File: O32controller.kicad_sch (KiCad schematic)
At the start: 25 parts, among them J1 Conn_01x08_MountingPin, J2 BATT+, J3 BATT-, J7 BATT+, J8 BATT-, U1 AS5047D, U2 STSPIN32F0A

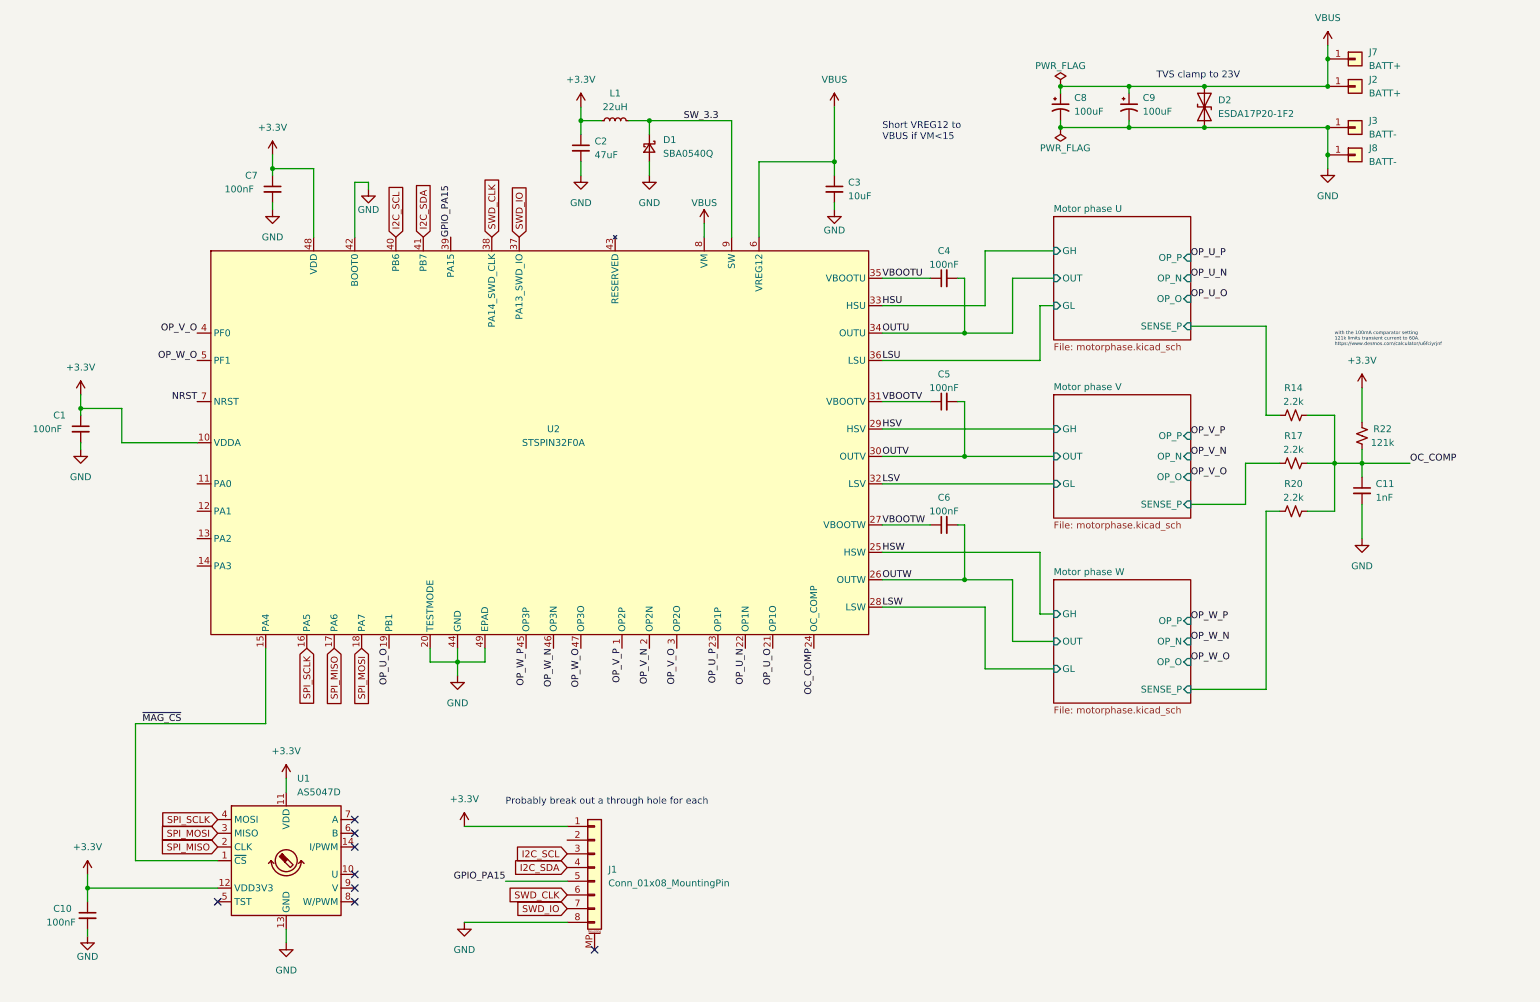
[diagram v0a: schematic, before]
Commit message: assigned gpio and adcs
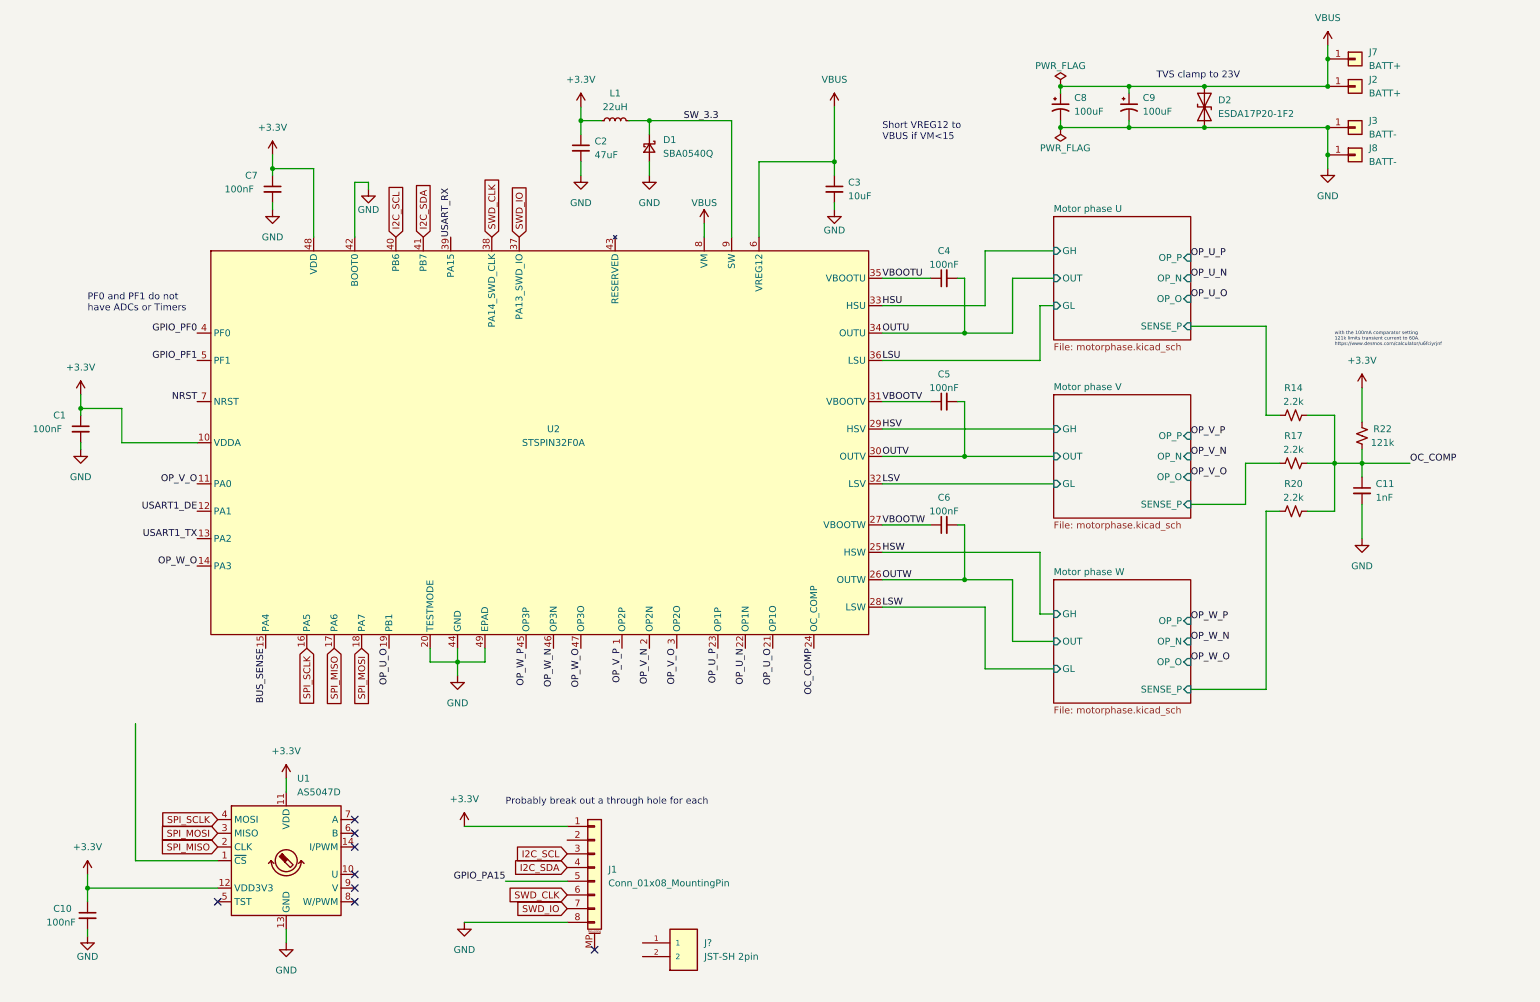
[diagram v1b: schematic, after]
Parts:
- added J?: JST-SH 2pin, SM02B-SRSS-TB(LF)(SN), symbol O32controller:SM02B-SRSS-TB(LF)(SN)
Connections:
- net GPIO_PA15: no longer U2.39 (PA15)
- net OP_V_O: now also U2.11 (PA0); no longer U2.4 (PF0)
- net OP_W_O: now also U2.14 (PA3); no longer U2.5 (PF1)
- net USART1_DE: now reaches U2.12 (PA1)
- net USART1_TX: now reaches U2.13 (PA2)
- net ~{MAG_CS}: no longer names the net of U1.1 (~{CS})
- net ~{MAG_CS}: no longer U2.15 (PA4)
- new net BUS_SENSE: U2.15 (PA4)
- new net GPIO_PF0: U2.4 (PF0)
- new net GPIO_PF1: U2.5 (PF1)
- new net USART_RX: U2.39 (PA15)
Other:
- note added: "PF0 and PF1 do not have ADCs or Timers"
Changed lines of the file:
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@@
-    (stroke (width 0) (type default) (color 0 0 0 0))
-  )
-  (wire (pts (xy 58.42 146.05) (xy 58.42 132.08))
     (stroke (width 0) (type default) (color 0 0 0 0))
   )
@@
     (stroke (width 0) (type default) (color 0 0 0 0))
   )
-  (wire (pts (xy 34.29 146.05) (xy 58.42 146.05))
-    (stroke (width 0) (type default) (color 0 0 0 0))
-  )
   (wire (pts (xy 204.47 130.81) (xy 196.85 130.81))
     (stroke (width 0) (type default) (color 0 0 0 0))
@@
   (wire (pts (xy 172.72 91.44) (xy 204.47 91.44))
     (stroke (width 0) (type default) (color 0 0 0 0))
+  )
+  (text "PF0 and PF1 do not \nhave ADCs or Timers\n" (at 25.4 69.85 0)
+    (effects (font (size 1.27 1.27)) (justify left bottom))
   )
   (text "Short VREG12 to \nVBUS if VM<15" (at 172.72 38.1 0)
@@
     (effects (font (size 1.27 1.27)) (justify right bottom))
   )
-  (label "OP_W_O" (at 45.72 78.74 180)
-    (effects (font (size 1.27 1.27)) (justify right bottom))
-  )
   (label "OP_V_N" (at 229.87 96.52 0)
     (effects (font (size 1.27 1.27)) (justify left bottom))
@@
     (effects (font (size 1.27 1.27)) (justify left bottom))
   )
-  (label "GPIO_PA15" (at 92.71 55.88 90)
-    (effects (font (size 1.27 1.27)) (justify left bottom))
-  )
   (label "OC_COMP" (at 160.02 132.08 270)
     (effects (font (size 1.27 1.27)) (justify right bottom))
@@
     (effects (font (size 1.27 1.27)) (justify left bottom))
   )
+  (label "GPIO_PF1" (at 45.72 78.74 180)
+    (effects (font (size 1.27 1.27)) (justify right bottom))
+  )
+  (label "USART1_DE" (at 45.72 106.68 180)
+    (effects (font (size 1.27 1.27)) (justify right bottom))
+  )
   (label "VBOOTW" (at 172.72 109.22 0)
     (effects (font (size 1.27 1.27)) (justify left bottom))
   )
+  (label "BUS_SENSE" (at 58.42 132.08 270)
+    (effects (font (size 1.27 1.27)) (justify right bottom))
+  )
   (label "NRST" (at 45.72 86.36 180)
     (effects (font (size 1.27 1.27)) (justify right bottom))
   )
+  (label "GPIO_PF0" (at 45.72 73.66 180)
+    (effects (font (size 1.27 1.27)) (justify right bottom))
+  )
   (label "LSU" (at 172.72 78.74 0)
     (effects (font (size 1.27 1.27)) (justify left bottom))
@@
     (effects (font (size 1.27 1.27)) (justify left bottom))
   )
-  (label "~{MAG_CS}" (at 35.56 146.05 0)
-    (effects (font (size 1.27 1.27)) (justify left bottom))
-  )
   (label "HSU" (at 172.72 68.58 0)
     (effects (font (size 1.27 1.27)) (justify left bottom))
   )
+  (label "USART_RX" (at 92.71 55.88 90)
+    (effects (font (size 1.27 1.27)) (justify left bottom))
+  )
   (label "OP_U_O" (at 152.4 132.08 270)
     (effects (font (size 1.27 1.27)) (justify right bottom))
@@
     (effects (font (size 1.27 1.27)) (justify left bottom))
   )
+  (label "OP_W_O" (at 45.72 116.84 180)
+    (effects (font (size 1.27 1.27)) (justify right bottom))
+  )
   (label "VBOOTV" (at 172.72 86.36 0)
     (effects (font (size 1.27 1.27)) (justify left bottom))
@@
     (effects (font (size 1.27 1.27)) (justify left bottom))
   )
-  (label "OP_V_O" (at 45.72 73.66 180)
+  (label "OP_V_O" (at 45.72 101.6 180)
     (effects (font (size 1.27 1.27)) (justify right bottom))
   )
@@
   (label "OUTW" (at 172.72 119.38 0)
     (effects (font (size 1.27 1.27)) (justify left bottom))
+  )
+  (label "USART1_TX" (at 45.72 111.76 180)
+    (effects (font (size 1.27 1.27)) (justify right bottom))
   )
   (global_label "SWD_IO" (shape input) (at 114.3 180.34 180) (fields_autoplaced)
@@
     (pin "MP")
   )
+  (symbol (lib_id "O32controller:SM02B-SRSS-TB(LF)(SN)") (at 128.27 191.77 0) (unit 1)
+    (in_bom yes) (on_board yes) (fields_autoplaced)
+    (property "Reference" "J?" (id 0) (at 139.7 186.6899 0)
+      (effects (font (size 1.27 1.27)) (justify left))
+    )
+    (property "Value" "JST-SH 2pin" (id 1) (at 139.7 189.2299 0)
+      (effects (font (size 1.27 1.27)) (justify left))
+    )
+    (property "Footprint" "SM02B-SRSS-TB(LF)(SN)" (id 2) (at 128.27 196.85 0)
+      (effects (font (size 1.27 1.27)) (justify bottom) hide)
+    )
+    (property "Datasheet" "" (id 3) (at 128.27 191.77 0)
+      (effects (font (size 1.27 1.27)) hide)
+    )
+    (property "MP" "SM02B-SRSS-TB_LF__SN_" (id 4) (at 128.27 199.39 0)
+      (effects (font (size 1.27 1.27)) (justify bottom) hide)
+    )
+    (property "PACKAGE" "None" (id 5) (at 135.89 201.93 0)
+      (effects (font (size 1.27 1.27)) (justify bottom) hide)
+    )
+    (property "PRICE" "0.23 USD" (id 6) (at 123.19 201.93 0)
+      (effects (font (size 1.27 1.27)) (justify bottom) hide)
+    )
+    (property "AVAILABILITY" "Good" (id 7) (at 140.97 201.93 0)
+      (effects (font (size 1.27 1.27)) (justify bottom) hide)
+    )
+    (property "MF" "JST" (id 8) (at 130.81 201.93 0)
+      (effects (font (size 1.27 1.27)) (justify bottom) hide)
+    )
+    (property "DESCRIPTION" "SH Series 2 Position 1 mm Pitch Surface Mount Side Entry Shrouded Header" (id 9) (at 128.27 194.31 0)
+      (effects (font (size 1.27 1.27)) (justify bottom) hide)
+    )
+    (pin "1")
+    (pin "2")
+  )
   (symbol (lib_id "power:+3.3V") (at 95.25 165.1 0) (unit 1)
     (in_bom yes) (on_board yes) (fields_autoplaced)
@@
       (reference "J8") (unit 1) (value "BATT-") (footprint "O32controller:SolderWire-Actual_1x01_D1.7mm_OD_2.75mm")
     )
+    (path "/a4996fed-2569-43a9-b3ce-0da5c184b86c"
+      (reference "J?") (unit 1) (value "JST-SH 2pin") (footprint "SM02B-SRSS-TB(LF)(SN)")
+    )
     (path "/6c4baef6-fdf2-4afa-9619-12d184d04052"

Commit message: added mag702, leds, thought about tx out:
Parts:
- removed J1: Conn_01x08_MountingPin, Connector_Molex:Molex_PicoBlade_53261-0871_1x08-1MP_P1.25mm_Horizontal, symbol Connector_Generic_MountingPin:Conn_01x08_MountingPin
- removed J?: JST-SH 2pin, SM02B-SRSS-TB(LF)(SN), symbol O32controller:SM02B-SRSS-TB(LF)(SN)
- removed U1: AS5047D, Package_SO:TSSOP-14_4.4x5mm_P0.65mm, symbol Sensor_Magnetic:AS5047D
- added D3: RED, symbol Device:LED
- added D4: GREEN, symbol Device:LED
- added D?: PMEG4010ESB, symbol Device:D_Schottky_Small
- added D?: PMEG4010ESB, O32controller:SDM2U30CSP-7, symbol Device:D_Schottky_Small
- added J1: SWD Connector, O32controller:JST_SM04B-SRSS-TB(LF)(SN), symbol O32controller:JST_SM04B-SRSS-TB(LF)(SN)
- added J12: I2C/RS485_2, O32controller:JST_SM02B-SRSS-TB(LF)(SN), symbol O32controller:JST_SM02B-SRSS-TB(LF)(SN)
- added J9: I2C/RS485_1, O32controller:JST_SM02B-SRSS-TB(LF)(SN), symbol O32controller:JST_SM02B-SRSS-TB(LF)(SN)
- added NT4: SDA/A, NetTie:NetTie-small, symbol Device:NetTie_2
- added NT5: SCL/B, NetTie:NetTie-small, symbol Device:NetTie_2
- added R26: 40k, symbol Device:R_Small_US
- added R27: 10k, symbol Device:R_Small_US
- added R28, R?: 1k, symbol Device:R_Small_US
- added TP1, TP2: TestPoint, symbol Connector:TestPoint
- added U1: MA702GQ-P, O32controller:MA702GQ-P, symbol O32controller:MA702GQ-P
- C10: value 100nF -> 1uF
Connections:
- net +3.3V: now also D4.2 (A), R28.2, U1.13 (VDD)
- net BUS_SENSE: now also R26.2, R27.1, TP2.1
- net GND: now also D3.1 (K), J1.4, J1.S1 (SHIELD), J1.S2 (SHIELD), J12.S1 (Shield), J12.S2 (Shield), J9.S1 (Shield), J9.S2 (Shield), R27.2, R?.2, U1.10 (TEST), U1.17 (PAD), U1.8 (GND)
- net I2C_SCL: now also NT5.1
- net I2C_SDA: now also NT4.1
- net NRST: now also TP1.1
- net SPI_MISO: now also U1.7 (MISO)
- net SPI_MOSI: now also U1.4 (MOSI)
- net SPI_SCLK: now also U1.12 (SCLK)
- net SWD_CLK: now also J1.3
- net SWD_IO: now also J1.2
- net USART1_TX: now also J1.1
- net VBUS: now also R26.1
- net GPIO_PF0 renamed LED_STATUS
- net LED_STATUS: now also D?.1 (K), D?.2 (A)
- net GPIO_PF1 renamed ~{MAG_CS}
- net ~{MAG_CS}: now also U1.5 (CS)
- new net: D4.1 (K), D?.1 (K), R?.1
- new net: D3.2 (A), D?.2 (A), R28.1
- new net RS485_A: J12.1, J9.1, NT4.2
- new net RS485_B: J12.2, J9.2, NT5.2
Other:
- note added: "Don't need diodes because if VBUS>15 or VBUS<0 then we got other problems"
- note added: "Must apply VBUS when using SWD"
- note added: "RED on when high-Z or HIGH GREEN on when LOW"
- note removed: "Probably break out a through hole for each"
- moved on the sheet: C1, C10, C11, C2, C3, C4, C5, C6, C7, C8, C9, D1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
